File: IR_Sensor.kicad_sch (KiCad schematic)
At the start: 33 parts, among them J8 Conn_01x03_Female, Q1 AO3401, Q3 NJL7302L-F3, Q31 Q_NPN_BEC, U12 AE-BME280, U17 OSRB38C9AA

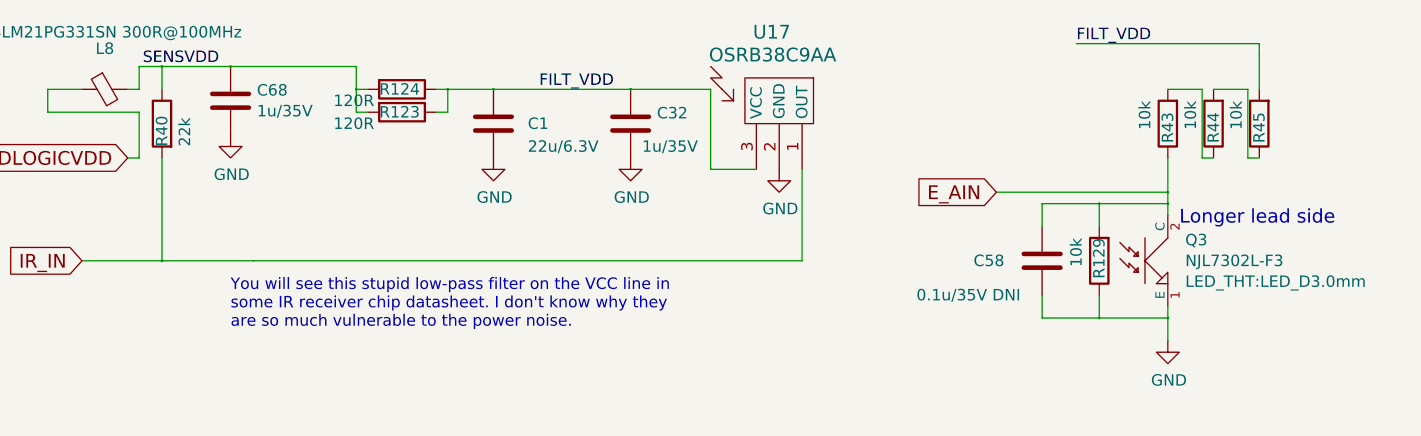
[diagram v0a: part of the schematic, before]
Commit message: Re-arranged physical buttions; DRC clear
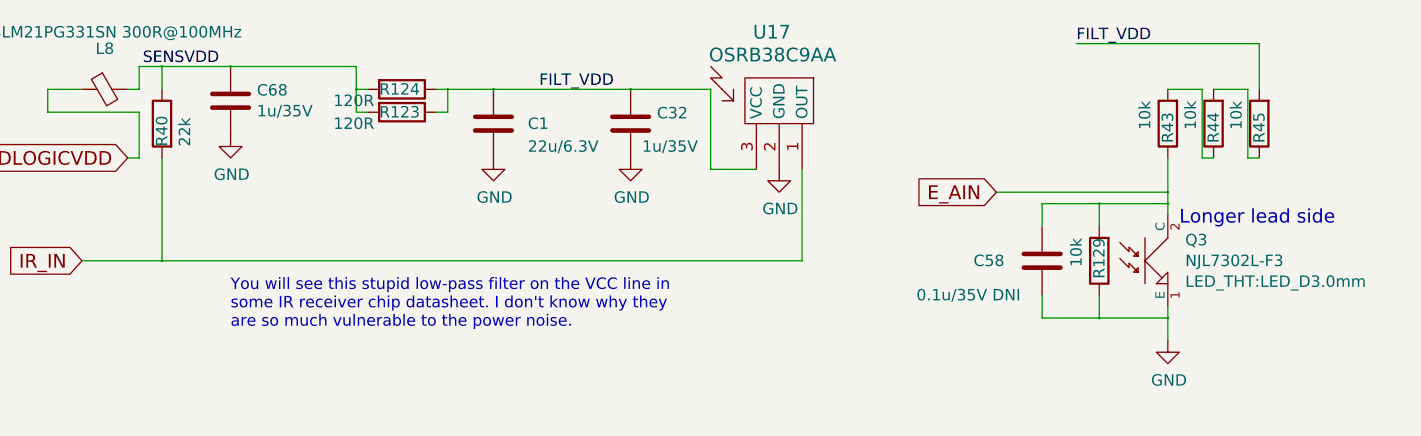
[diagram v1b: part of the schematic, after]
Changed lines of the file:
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@@
-(kicad_sch (version 20200827) (generator eeschema)
+(kicad_sch (version 20200828) (generator eeschema)
   (page 2 10)
   (paper "A4")
@@
     (stroke (width 0) (type solid) (color 0 0 0 0))
   )
-  (wire (pts (xy 34.29 39.37) (xy 44.45 39.37))
+  (wire (pts (xy 34.29 39.37) (xy 105.41 39.37))
     (stroke (width 0) (type solid) (color 0 0 0 0))
   )
@@
     (stroke (width 0) (type solid) (color 0 0 0 0))
   )
-  (wire (pts (xy 105.41 39.37) (xy 44.45 39.37))
-    (stroke (width 0) (type solid) (color 0 0 0 0))
-  )
   (wire (pts (xy 111.76 83.82) (xy 121.92 83.82))
     (stroke (width 0) (type solid) (color 0 0 0 0))
@@
     (stroke (width 0) (type solid) (color 0 0 0 0))
   )
-  (wire (pts (xy 156.21 15.24) (xy 156.21 16.51))
-    (stroke (width 0) (type solid) (color 0 0 0 0))
-  )
-  (wire (pts (xy 156.21 16.51) (xy 156.21 20.32))
-    (stroke (width 0) (type solid) (color 0 0 0 0))
-  )
+  (wire (pts (xy 156.21 15.24) (xy 156.21 20.32))
+    (stroke (width 0) (type solid) (color 0 0 0 0))
+  )

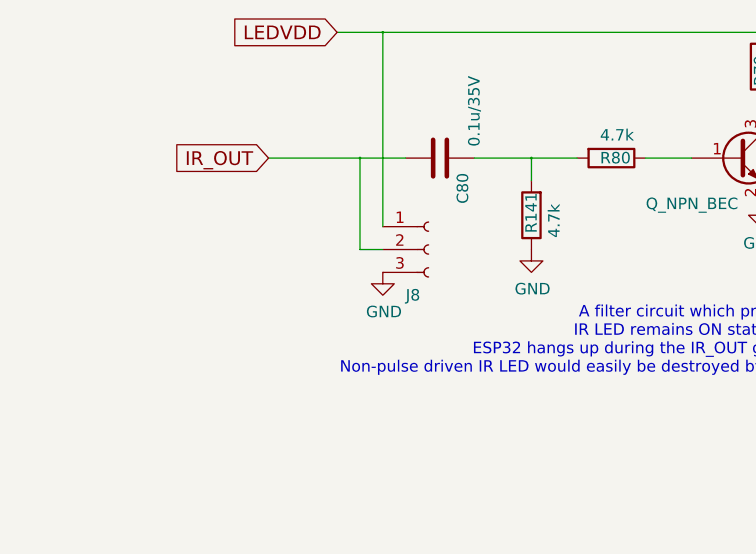
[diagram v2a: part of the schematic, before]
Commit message: Added J8.4; DRC clear
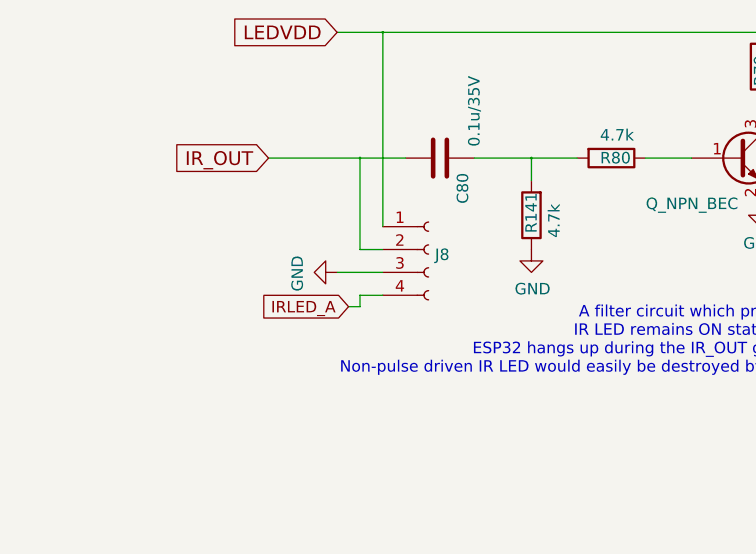
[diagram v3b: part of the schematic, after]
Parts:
- removed J8: Conn_01x03_Female, Connector_PinHeader_2.54mm:PinHeader_1x03_P2.54mm_Vertical, symbol dotmatrix_64x48-rescue:Conn_01x03_Female-Connector
- added J8: Conn_01x04_Female, Connector_PinSocket_2.54mm:PinSocket_1x04_P2.54mm_Vertical, symbol Connector:Conn_01x04_Female
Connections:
- net GND: now also J8.3 (Pin_3)
- net IRLED_A: now also J8.4 (Pin_4)
- net IR_OUT: now also J8.2 (Pin_2)
- net LEDVDD: now also J8.1 (Pin_1)
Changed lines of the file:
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@@
+    (stroke (width 0) (type solid) (color 0 0 0 0))
+  )
+  (wire (pts (xy 44.45 96.52) (xy 49.53 96.52))
+    (stroke (width 0) (type solid) (color 0 0 0 0))
+  )
+  (wire (pts (xy 45.72 100.33) (xy 46.99 100.33))
     (stroke (width 0) (type solid) (color 0 0 0 0))
   )
@@
   )
   (wire (pts (xy 46.99 93.98) (xy 49.53 93.98))
+    (stroke (width 0) (type solid) (color 0 0 0 0))
+  )
+  (wire (pts (xy 46.99 99.06) (xy 49.53 99.06))
+    (stroke (width 0) (type solid) (color 0 0 0 0))
+  )
+  (wire (pts (xy 46.99 100.33) (xy 46.99 99.06))
     (stroke (width 0) (type solid) (color 0 0 0 0))
   )
@@
     (effects (font (size 1.524 1.524)) (justify right))
   )
+  (global_label "IRLED_A" (shape input) (at 45.72 100.33 180)
+    (effects (font (size 1.27 1.27)) (justify right))
+  )
   (global_label "E_AIN" (shape input) (at 127 31.75 180)
     (effects (font (size 1.524 1.524)) (justify right))
@@
     (property "Datasheet" "" (id 3) (at 41.91 25.4 0))
   )
-  (symbol (lib_id "dotmatrix_64x48-rescue:GND-power") (at 49.53 96.52 0) (unit 1)
-    (in_bom yes) (on_board yes)
-    (property "Reference" "#PWR0138" (id 0) (at 49.53 102.87 0)
-      (effects (font (size 1.27 1.27)) hide)
-    )
-    (property "Value" "GND" (id 1) (at 49.657 100.9142 0))
-    (property "Footprint" "" (id 2) (at 49.53 96.52 0))
-    (property "Datasheet" "" (id 3) (at 49.53 96.52 0))
+  (symbol (lib_id "dotmatrix_64x48-rescue:GND-power") (at 44.45 96.52 270) (unit 1)
+    (in_bom yes) (on_board yes)
+    (property "Reference" "#PWR0138" (id 0) (at 38.1 96.52 0)
+      (effects (font (size 1.27 1.27)) hide)
+    )
+    (property "Value" "GND" (id 1) (at 40.0558 96.647 0))
+    (property "Footprint" "" (id 2) (at 44.45 96.52 0))
+    (property "Datasheet" "" (id 3) (at 44.45 96.52 0))
   )
   (symbol (lib_id "dotmatrix_64x48-rescue:GND-power") (at 66.04 93.98 0) (unit 1)
@@
     (property "Datasheet" "" (id 3) (at 191.77 41.91 0))
   )
-  (symbol (lib_id "dotmatrix_64x48-rescue:Conn_01x03_Female-Connector") (at 54.61 93.98 0) (unit 1)
-    (in_bom yes) (on_board yes)
-    (property "Reference" "J8" (id 0) (at 52.07 99.06 0)
-      (effects (font (size 1.27 1.27)) (justify left))
-    )
-    (property "Value" "Conn_01x03_Female" (id 1) (at 39.37 87.63 0)
-      (effects (font (size 1.27 1.27)) (justify left) hide)
-    )
-    (property "Footprint" "Connector_PinHeader_2.54mm:PinHeader_1x03_P2.54mm_Vertical" (id 2) (at 54.61 93.98 0)
-      (effects (font (size 1.27 1.27)) hide)
-    )
-    (property "Datasheet" "" (id 3) (at 54.61 93.98 0)
-      (effects (font (size 1.27 1.27)) hide)
-    )
+  (symbol (lib_id "Connector:Conn_01x04_Female") (at 54.61 93.98 0) (unit 1)
+    (in_bom yes) (on_board yes)
+    (property "Reference" "J8" (id 0) (at 55.321 94.558 0)
+      (effects (font (size 1.27 1.27)) (justify left))
+    )
+    (property "Value" "Conn_01x04_Female" (id 1) (at 55.321 96.857 0)
+      (effects (font (size 1.27 1.27)) (justify left) hide)
+    )
+    (property "Footprint" "Connector_PinSocket_2.54mm:PinSocket_1x04_P2.54mm_Vertical" (id 2) (at 54.61 93.98 0)
+      (effects (font (size 1.27 1.27)) hide)
+    )
+    (property "Datasheet" "~" (id 3) (at 54.61 93.98 0)
+      (effects (font (size 1.27 1.27)) hide)
+    )

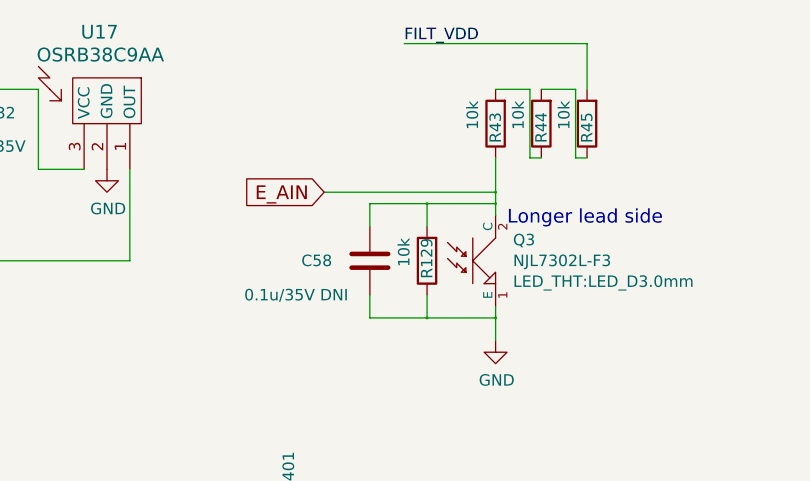
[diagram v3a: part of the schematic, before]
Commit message: Moved leftside sensors to rightside; Unified old footprints to new footprints; DRC clear
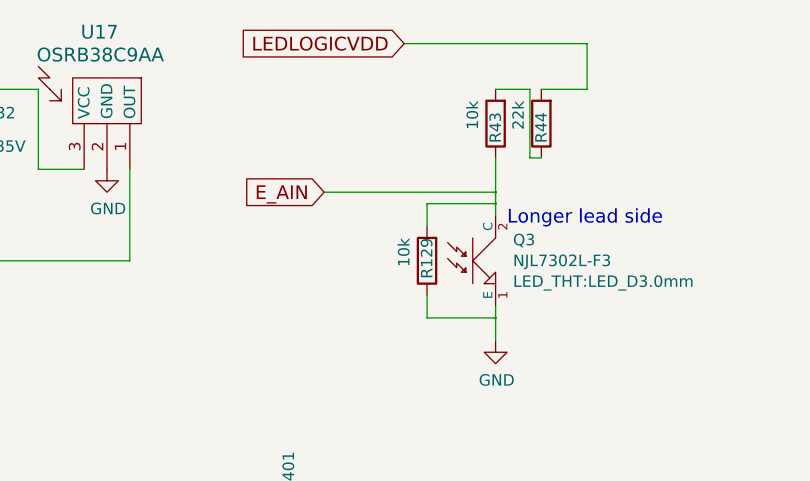
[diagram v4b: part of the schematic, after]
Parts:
- removed C58: 0.1u/35V DNI, Capacitor_SMD:C_0603_1608Metric_Pad1.05x0.95mm_HandSolder, symbol dotmatrix_64x48-rescue:C-device
- removed R45: 10k, Resistor_SMD:R_0603_1608Metric_Pad1.05x0.95mm_HandSolder, symbol dotmatrix_64x48-rescue:R-device
- Q1: footprint TO_SOT_Packages_SMD:SOT-23_Handsoldering -> Package_TO_SOT_SMD:SOT-23_Handsoldering
- R44: value 10k -> 22k
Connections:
- net LEDLOGICVDD: now also R44.2
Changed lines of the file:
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@@
   (junction (at 114.3 69.85) (diameter 0.3048) (color 0 0 0 0))
   (junction (at 129.54 69.85) (diameter 0.3048) (color 0 0 0 0))
-  (junction (at 138.43 33.02) (diameter 0.3048) (color 0 0 0 0))
-  (junction (at 138.43 45.72) (diameter 0.3048) (color 0 0 0 0))
   (junction (at 144.78 69.85) (diameter 0.3048) (color 0 0 0 0))
   (junction (at 146.05 31.75) (diameter 0.3048) (color 0 0 0 0))
@@
     (stroke (width 0) (type solid) (color 0 0 0 0))
   )
-  (wire (pts (xy 132.08 33.02) (xy 132.08 35.56))
-    (stroke (width 0) (type solid) (color 0 0 0 0))
-  )
-  (wire (pts (xy 132.08 33.02) (xy 138.43 33.02))
-    (stroke (width 0) (type solid) (color 0 0 0 0))
-  )
-  (wire (pts (xy 132.08 43.18) (xy 132.08 45.72))
-    (stroke (width 0) (type solid) (color 0 0 0 0))
-  )
-  (wire (pts (xy 132.08 45.72) (xy 138.43 45.72))
-    (stroke (width 0) (type solid) (color 0 0 0 0))
-  )
   (wire (pts (xy 135.89 15.24) (xy 156.21 15.24))
     (stroke (width 0) (type solid) (color 0 0 0 0))
@@
     (stroke (width 0) (type solid) (color 0 0 0 0))
   )
-  (wire (pts (xy 154.94 27.94) (xy 154.94 20.32))
+  (wire (pts (xy 154.94 20.32) (xy 156.21 20.32))
     (stroke (width 0) (type solid) (color 0 0 0 0))
   )
   (wire (pts (xy 156.21 15.24) (xy 156.21 20.32))
-    (stroke (width 0) (type solid) (color 0 0 0 0))
-  )
-  (wire (pts (xy 156.21 27.94) (xy 154.94 27.94))
     (stroke (width 0) (type solid) (color 0 0 0 0))
   )
@@
     (effects (font (size 1.27 1.27)) (justify left bottom))
   )
-  (label "FILT_VDD" (at 135.89 15.24 0)
-    (effects (font (size 1.27 1.27)) (justify left bottom))
-  )
   (global_label "IR_IN" (shape input) (at 25.4 39.37 180)
     (effects (font (size 1.524 1.524)) (justify right))
@@
   )
   (global_label "E_AIN" (shape input) (at 127 31.75 180)
+    (effects (font (size 1.524 1.524)) (justify right))
+  )
+  (global_label "LEDLOGICVDD" (shape input) (at 135.89 15.24 180)
     (effects (font (size 1.524 1.524)) (justify right))
   )
@@
       (effects (font (size 1.27 1.27)) (justify left))
     )
-    (property "Value" "10k" (id 1) (at 148.59 21.59 90)
+    (property "Value" "22k" (id 1) (at 148.59 21.59 90)
       (effects (font (size 1.27 1.27)) (justify left))
     )
@@
     )
     (property "Datasheet" "" (id 3) (at 153.67 77.47 0))
-  )
-  (symbol (lib_id "dotmatrix_64x48-rescue:R-device") (at 156.21 24.13 180) (unit 1)
-    (in_bom yes) (on_board yes)
-    (property "Reference" "R45" (id 0) (at 156.21 22.86 90)
-      (effects (font (size 1.27 1.27)) (justify left))
-    )
-    (property "Value" "10k" (id 1) (at 153.67 21.59 90)
-      (effects (font (size 1.27 1.27)) (justify left))
-    )
-    (property "Footprint" "Resistor_SMD:R_0603_1608Metric_Pad1.05x0.95mm_HandSolder" (id 2) (at 157.988 24.13 90)
-      (effects (font (size 1.27 1.27)) hide)
-    )
-    (property "Datasheet" "" (id 3) (at 156.21 24.13 0))
   )
   (symbol (lib_id "dotmatrix_64x48-rescue:R-device") (at 156.21 77.47 180) (unit 1)
@@
     (property "Datasheet" "" (id 3) (at 114.3 73.66 0))
   )
-  (symbol (lib_id "dotmatrix_64x48-rescue:C-device") (at 132.08 39.37 0) (unit 1)
-    (in_bom yes) (on_board yes)
-    (property "Reference" "C58" (id 0) (at 124.46 39.37 0)
-      (effects (font (size 1.27 1.27)) (justify left))
-    )
-    (property "Value" "0.1u/35V DNI" (id 1) (at 118.11 43.18 0)
-      (effects (font (size 1.27 1.27)) (justify left))
-    )
-    (property "Footprint" "Capacitor_SMD:C_0603_1608Metric_Pad1.05x0.95mm_HandSolder" (id 2) (at 135.001 41.6814 0)
-      (effects (font (size 1.27 1.27)) (justify left) hide)
-    )
-    (property "Datasheet" "" (id 3) (at 132.08 39.37 0))
-  )
   (symbol (lib_id "dotmatrix_64x48-rescue:C-device") (at 191.77 41.91 270) (unit 1)
     (in_bom yes) (on_board yes)
@@
       (effects (font (size 1.27 1.27)) (justify left))
     )
-    (property "Footprint" "TO_SOT_Packages_SMD:SOT-23_Handsoldering" (id 2) (at 124.46 67.31 0)
-      (effects (font (size 1.27 1.27)) hide)
-    )
+    (property "Footprint" "Package_TO_SOT_SMD:SOT-23_Handsoldering" (id 2) (at 124.46 67.31 0)
+      (effects (font (size 1.27 1.27)) hide)
+    )

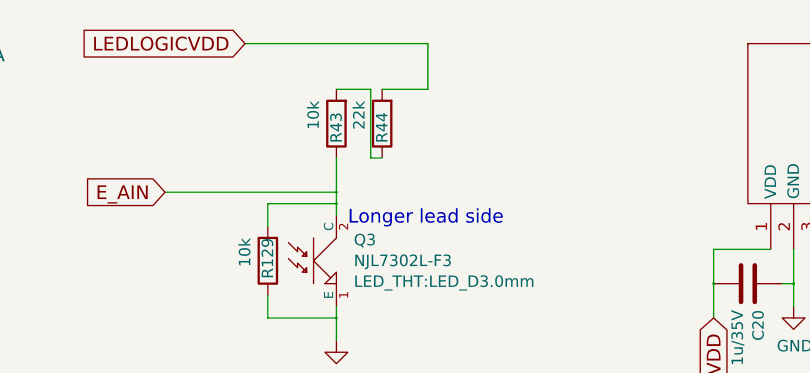
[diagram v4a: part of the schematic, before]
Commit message: Changed LDO to one which has more lower drop voltage; DRC clear
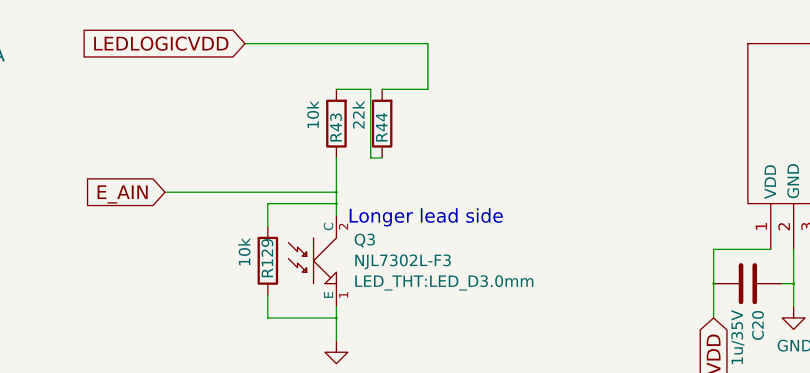
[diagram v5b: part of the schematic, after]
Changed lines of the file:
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@@
+    (stroke (width 0) (type solid) (color 0 0 0 0))
+  )
+  (wire (pts (xy 151.13 20.32) (xy 156.21 20.32))
     (stroke (width 0) (type solid) (color 0 0 0 0))
   )
@@
     (stroke (width 0) (type solid) (color 0 0 0 0))
   )
-  (wire (pts (xy 154.94 20.32) (xy 151.13 20.32))
-    (stroke (width 0) (type solid) (color 0 0 0 0))
-  )
-  (wire (pts (xy 154.94 20.32) (xy 156.21 20.32))
-    (stroke (width 0) (type solid) (color 0 0 0 0))
-  )

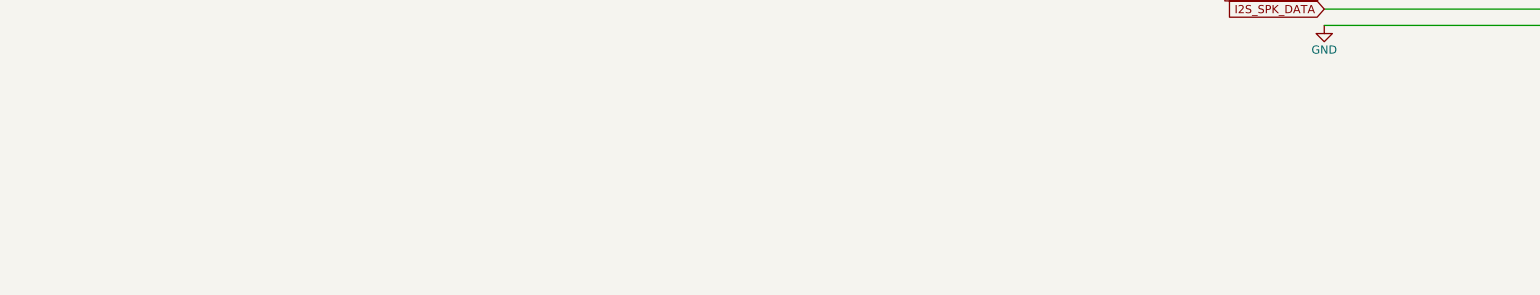
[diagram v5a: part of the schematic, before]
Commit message: To use WS2812-2020 as status LEDs; No critical DRC errors found
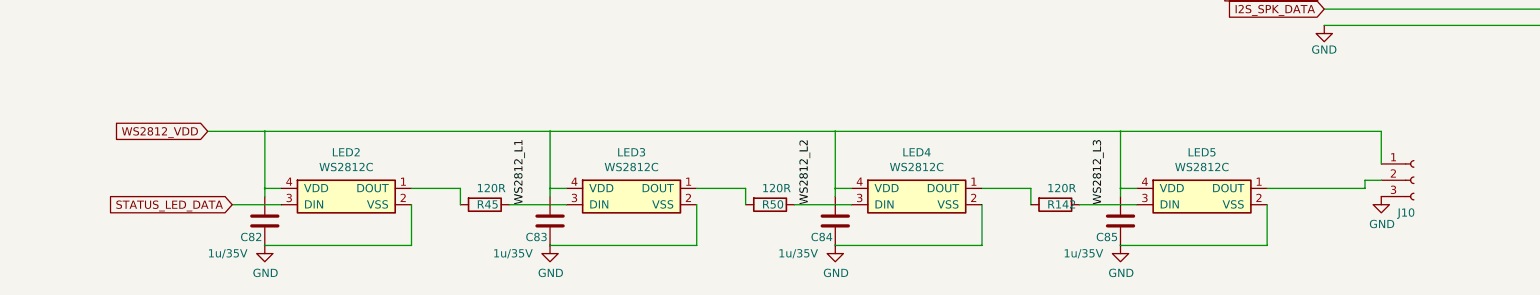
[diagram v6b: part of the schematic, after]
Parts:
- added C82, C83, C84, C85: 1u/35V, Capacitor_SMD:C_0603_1608Metric_Pad1.08x0.95mm_HandSolder, symbol dotmatrix_64x48-rescue:C-device
- added J10: Conn_01x03_Female, Connector_PinHeader_2.54mm:PinHeader_1x03_P2.54mm_Vertical, symbol dotmatrix_64x48-rescue:Conn_01x03_Female-Connector
- added LED2, LED3, LED4, LED5: WS2812C, components:WS2812C_2x2mm, symbol DeeComponents:WS2812C
- added R142, R45, R50: 120R, Resistor_SMD:R_0603_1608Metric_Pad0.98x0.95mm_HandSolder, symbol dotmatrix_64x48-rescue:R-device
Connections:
- net GND: now also C82.2, C83.2, C84.2, C85.2, J10.3 (Pin_3), LED2.2 (VSS), LED3.2 (VSS), LED4.2 (VSS), LED5.2 (VSS)
- new net: LED3.1 (DOUT), R50.2
- new net: J10.2 (Pin_2), LED5.1 (DOUT)
- new net: LED2.1 (DOUT), R45.2
- new net: LED4.1 (DOUT), R142.2
- new net STATUS_LED_DATA: LED2.3 (DIN)
- new net WS2812_L1: LED3.3 (DIN), R45.1
- new net WS2812_L2: LED4.3 (DIN), R50.1
- new net WS2812_L3: LED5.3 (DIN), R142.1
- new net WS2812_VDD: C82.1, C83.1, C84.1, C85.1, J10.1 (Pin_1), LED2.4 (VDD), LED3.4 (VDD), LED4.4 (VDD), LED5.4 (VDD)
